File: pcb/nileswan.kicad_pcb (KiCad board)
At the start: 4 copper layers, 61.2 x 36.6 mm, 54 parts, among them J1 Micro_SD_Card_Det_Hirose_DM3AT, J2 Conn_01x06, U1 ICE40HX1K-VQ100, U2 W25Q16JVZPIQ, U3 AP2127N-1.2, U4 IS66WVE4M16EBLL-70BLI, Y1 AMPMAFB-25.0000T

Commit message: current erata, ibom and PCB changes necessary to manufacture it
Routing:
- net GND: vias 47 -> 49
- added copper zone on B.Cu, net GND
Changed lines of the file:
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@@
   (via (at 144.44 87.14) (size 0.5) (drill 0.3) (layers "F.Cu" "B.Cu") (net 1))
   (via (at 171 96) (size 0.5) (drill 0.3) (layers "F.Cu" "B.Cu") (net 1))
+  (via (at 158.56 96.01) (size 0.5) (drill 0.3) (layers "F.Cu" "B.Cu") (free) (net 1))
   (via (at 172.6 110.3) (size 0.5) (drill 0.3) (layers "F.Cu" "B.Cu") (net 1))
   (via (at 133.1 98.827) (size 0.5) (drill 0.3) (layers "F.Cu" "B.Cu") (net 1))
@@
   (via (at 138.4 86.8) (size 0.5) (drill 0.3) (layers "F.Cu" "B.Cu") (net 1))
   (via (at 164.225 102.9) (size 0.5) (drill 0.3) (layers "F.Cu" "B.Cu") (net 1))
+  (via (at 160.87 98.13) (size 0.5) (drill 0.3) (layers "F.Cu" "B.Cu") (free) (net 1))
   (via (at 152.97 100.33) (size 0.5) (drill 0.3) (layers "F.Cu" "B.Cu") (net 1))
   (via (at 155.2 83.4) (size 0.5) (drill 0.3) (layers "F.Cu" "B.Cu") (net 1))
@@
   (via (at 158.7 93.8) (size 0.45) (drill 0.3) (layers "F.Cu" "B.Cu") (net 62))
   (via (at 128.9 88.5) (size 0.45) (drill 0.3) (layers "F.Cu" "B.Cu") (net 62))
+  (segment (start 157.544512 93.8) (end 156.835012 94.5095) (width 0.127) (layer "B.Cu") (net 62))
   (segment (start 134.4 94) (end 128.9 88.5) (width 0.127) (layer "B.Cu") (net 62))
-  (segment (start 157.92 94.58) (end 157.5765 94.2365) (width 0.127) (layer "B.Cu") (net 62))
+  (segment (start 147.008012 93.8365) (end 146.844512 94) (width 0.127) (layer "B.Cu") (net 62))
   (segment (start 156.835012 94.5095) (end 148.064988 94.5095) (width 0.127) (layer "B.Cu") (net 62))
-  (segment (start 147.008012 93.8365) (end 146.844512 94) (width 0.127) (layer "B.Cu") (net 62))
-  (segment (start 158.7 93.8) (end 157.92 94.58) (width 0.127) (layer "B.Cu") (net 62))
-  (segment (start 157.5765 94.2365) (end 157.108012 94.2365) (width 0.127) (layer "B.Cu") (net 62))
-  (segment (start 157.108012 94.2365) (end 156.835012 94.5095) (width 0.127) (layer "B.Cu") (net 62))
   (segment (start 146.844512 94) (end 134.4 94) (width 0.127) (layer "B.Cu") (net 62))
   (segment (start 147.391988 93.8365) (end 147.008012 93.8365) (width 0.127) (layer "B.Cu") (net 62))
   (segment (start 148.064988 94.5095) (end 147.391988 93.8365) (width 0.127) (layer "B.Cu") (net 62))
+  (segment (start 158.7 93.8) (end 157.544512 93.8) (width 0.127) (layer "B.Cu") (net 62))
   (segment (start 129.869 86.25) (end 130.1 86.25) (width 0.127) (layer "F.Cu") (net 63))
   (segment (start 158.182012 94.3375) (end 166.875 94.3375) (width 0.127) (layer "F.Cu") (net 63))
@@
   (via (at 136.3 98.9) (size 0.45) (drill 0.3) (layers "F.Cu" "B.Cu") (net 83))
   (via (at 165.1 98.3) (size 0.45) (drill 0.3) (layers "F.Cu" "B.Cu") (net 83))
+  (segment (start 152.328 103.238) (end 159.6 103.238) (width 0.127) (layer "B.Cu") (net 83))
+  (segment (start 138.3175 103.1175) (end 152.2075 103.1175) (width 0.127) (layer "B.Cu") (net 83))
+  (segment (start 136.3 101.1) (end 138.3175 103.1175) (width 0.127) (layer "B.Cu") (net 83))
   (segment (start 164.538 98.3) (end 165.1 98.3) (width 0.127) (layer "B.Cu") (net 83))
-  (segment (start 152.384 103.238) (end 159.6 103.238) (width 0.127) (layer "B.Cu") (net 83))
-  (segment (start 136.3 101.1) (end 138.3175 103.1175) (width 0.127) (layer "B.Cu") (net 83))
-  (segment (start 138.3175 103.1175) (end 151.0955 103.1175) (width 0.127) (layer "B.Cu") (net 83))
-  (segment (start 151.0955 103.1175) (end 151.8 103.822) (width 0.127) (layer "B.Cu") (net 83))
+  (segment (start 152.2075 103.1175) (end 152.328 103.238) (width 0.127) (layer "B.Cu") (net 83))
   (segment (start 159.6 103.238) (end 164.538 98.3) (width 0.127) (layer "B.Cu") (net 83))
   (segment (start 136.3 98.9) (end 136.3 101.1) (width 0.127) (layer "B.Cu") (net 83))
-  (segment (start 151.8 103.822) (end 152.384 103.238) (width 0.127) (layer "B.Cu") (net 83))
   (segment (start 163.75 84.25) (end 162.75 84.25) (width 0.127) (layer "F.Cu") (net 86))
   (segment (start 161.2125 88.562026) (end 161.2125 89.175) (width 0.127) (layer "F.Cu") (net 86))
@@
       )
     )
+  )
+  (zone (net 1) (net_name "GND") (layer "B.Cu") (hatch edge 0.5)
+    (priority 2)
+    (connect_pads (clearance 0.5))
+    (min_thickness 0.25) (filled_areas_thickness no)
+    (fill yes (thermal_gap 0.5) (thermal_bridge_width 0.5))
+    (polygon
+      (pts
+        (xy 107.18 77.99)
+        (xy 181.06 77.53)
+        (xy 179.07 121.57)
+        (xy 108.72 121.42)
+      )
+    )

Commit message: second pcb iteration
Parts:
- removed J2: Conn_01x06, Connector_PinSocket_1.27mm:PinSocket_1x06_P1.27mm_Vertical
- removed R14: 10k, Resistor_SMD:R_0603_1608Metric
- removed R20, R21: 2.2k, Resistor_SMD:R_0603_1608Metric
- added C24: 1 μF, Capacitor_SMD:C_0603_1608Metric, F.Cu at (163.1, 106.2)
- added C25: 1 μF, Capacitor_SMD:C_0603_1608Metric, F.Cu at (159.7, 102.7)
- added C26: 100 nF, Capacitor_SMD:C_0402_1005Metric, F.Cu at (129.0, 88.8)
- added C27: 470 pF, Capacitor_SMD:C_0402_1005Metric, F.Cu at (165.1, 103.2)
- added C28: 4.7 nF, Capacitor_SMD:C_0402_1005Metric, F.Cu at (165.1, 104.2)
- added C29: 100 nF, Capacitor_SMD:C_0402_1005Metric, F.Cu at (127.6, 85.5)
- added C30: 100 nF, Capacitor_SMD:C_0402_1005Metric, F.Cu at (125.5, 88.1)
- added C31: 100 nF, Capacitor_SMD:C_0402_1005Metric, F.Cu at (129.8, 97.2)
- added J3: SM02B-SRSS-TB_LF__SN_, snapeda:SM02B-SRSS-TB_LF__SN_, F.Cu at (133.9, 86.6)
- added J4: Conn_02x05_Counter_Clockwise, Connector:Tag-Connect_TC2050-IDC-NL_2x05_P1.27mm_Vertical, B.Cu at (133.4, 85.5)
- added R3: 47k, Resistor_SMD:R_0402_1005Metric, F.Cu at (163.4, 101.0)
- added R4: 10k, Resistor_SMD:R_0402_1005Metric, F.Cu at (145.1, 85.9)
- added R6: 10k, Resistor_SMD:R_0402_1005Metric, F.Cu at (139.3, 84.8)
- added R7: 10k, Resistor_SMD:R_0402_1005Metric, F.Cu at (159.4, 103.9)
- added R8: 2.2k, Resistor_SMD:R_0402_1005Metric, F.Cu at (156.1, 85.7)
- added U5: AP22966DC8-7, snapeda:IC_AP22966DC8-7, F.Cu at (162.5, 103.7)
- added U6: IS62WV5128EBLL-45BLI, nileswan:BGA-36_6x8_6.0x8.0mm, F.Cu at (129.4, 93.0)
- added U7: TPS3613, Package_SO:VSSOP-10_3x3mm_P0.5mm, F.Cu at (124.0, 85.4)
- C10, C12, C14, C15, C16, C17, C18, C19, C2, C20, C21, C22, C23, C3, C4, C5, C6, C7, C8, C9: footprint Capacitor_SMD:C_0603_1608Metric -> Capacitor_SMD:C_0402_1005Metric
- D1, D2, D3, D4, D5: footprint LED_SMD:LED_0603_1608Metric -> LED_SMD:LED_0402_1005Metric
- R10, R15, R16, R17, R2, R23, R9: footprint Resistor_SMD:R_0603_1608Metric -> Resistor_SMD:R_0402_1005Metric
- R11, R12, R13: value 10k -> 2.2k; footprint Resistor_SMD:R_0603_1608Metric -> Resistor_SMD:R_0402_1005Metric
- R18: value 2.2k -> 118k; footprint Resistor_SMD:R_0603_1608Metric -> Resistor_SMD:R_0402_1005Metric
- R19: value 2.2k -> 75k; footprint Resistor_SMD:R_0603_1608Metric -> Resistor_SMD:R_0402_1005Metric
- R5: value 47k -> 10k; footprint Resistor_SMD:R_0603_1608Metric -> Resistor_SMD:R_0402_1005Metric
- U2: value W25Q16JVZPIQ -> W25Q16JVUXIQ; footprint snapeda:SON127P500X600X80-9N -> snapeda:SON50P300X200X60-9N
- moved J1 42.8 mm to (165.1, 91.2), turned to 180 degrees
- moved R10 40.8 mm to (162.3, 101.0), turned to 90 degrees
- moved R9 38.7 mm to (156.2, 89.5), turned to -90 degrees
- moved R23 38.6 mm to (134.1, 104.2)
- moved C1 36.6 mm to (166.7, 101.1), turned to 0 degrees
- moved R5 33.5 mm to (145.6, 83.6)
- moved C11 30.9 mm to (158.2, 105.8), turned to 0 degrees
- moved U3 27.4 mm to (156.2, 104.8), turned to -90 degrees
- moved C15 26.9 mm to (141.1, 105.1), turned to -90 degrees
- moved C14 24.4 mm to (148.1, 86.0), turned to 90 degrees
- moved C13 24.2 mm to (153.7, 104.7)
- moved R15 22.0 mm to (156.1, 86.7)
- moved C19 20.7 mm to (137.0, 94.9), turned to 180 degrees
- moved R18 18.3 mm to (120.2, 84.7), turned to -90 degrees
- moved D1 17.6 mm to (154.0, 86.6), turned to 180 degrees
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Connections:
- net Net-(U1C-CRESET_B) renamed /fpga/CRESET_B
- net Net-(U3-VO) renamed 1.2V
- C1 pad 1: 3.3V -> 3.3V_TF
- J1 pad 10: /fpga/SD_DETECT -> /fpga/TF_DETECT
- J1 pad 2: Net-(J1-DAT3/CD) -> /fpga/TF_SEL
- J1 pad 3: /fpga/SD_CMD -> /fpga/TF_PICO
- J1 pad 4: 3.3V -> 3.3V_TF
- J1 pad 5: /fpga/SD_CLK -> /fpga/TF_CLK
- J1 pad 7: /fpga/SD_DAT0 -> /fpga/TF_POCI
- R1 pad 1: 3.3V -> Net-(U5-VBIAS)
- R10 pad 1: 3.3V -> 3.3V_TF
- R11 pad 1: 3.3V -> GND
- R11 pad 2: Net-(J2-Pin_3) -> Net-(D3-K)
- R12 pad 1: 3.3V -> GND
- R12 pad 2: Net-(U2-IO3) -> Net-(D4-K)
- R13 pad 1: 3.3V -> GND
- R13 pad 2: Net-(J2-Pin_4) -> Net-(D5-K)
- R15 pad 1: Net-(D1-K) -> GND
- R15 pad 2: GND -> Net-(D1-K)
- R18 pad 1: GND -> 3.3V
- R18 pad 2: Net-(D2-K) -> Net-(U7-SENSE)
- R19 pad 1: GND -> Net-(U7-SENSE)
- R19 pad 2: Net-(D3-K) -> GND
- R5 pad 2: Net-(J1-DAT1) -> Net-(U2-/WP)
- R9 pad 1: 3.3V -> 3.3V_TF
- R9 pad 2: Net-(J1-DAT3/CD) -> /fpga/TF_POCI
- U1 pad 1: /fpga/A_HIGH0 -> /fpga/A16
- U1 pad 10: /fpga/ENABLE_OUT_PSRAM -> /fpga/MBC
- U1 pad 100: unconnected-(U1A-IOT_95-Pad100) -> /fpga/A17
- U1 pad 12: /fpga/SD_DETECT -> /fpga//IO
- U1 pad 13: unconnected-(U1D-IOL_6B_GBIN7-Pad13) -> /fpga//WE
- U1 pad 15: unconnected-(U1D-IOL_7A_GBIN6-Pad15) -> /fpga/SCLK
- U1 pad 16: /fpga/SD_CMD -> /fpga//SEL
- U1 pad 18: /fpga/SD_DAT0 -> /fpga/TF_POW
- U1 pad 19: /fpga/SD_CLK -> /fpga/TF_SEL
- U1 pad 2: /fpga/A_HIGH1 -> /fpga/D8
- U1 pad 20: Net-(D2-A) -> /fpga/TF_PICO
- U1 pad 21: Net-(D3-A) -> /fpga/TF_CLK
- U1 pad 24: Net-(D4-A) -> /fpga/TF_POCI
- U1 pad 25: Net-(D5-A) -> /fpga/TF_DETECT
- U1 pad 26: unconnected-(U1C-IOB_26-Pad26) -> Net-(D2-A)
- U1 pad 27: unconnected-(U1C-IOB_27-Pad27) -> Net-(D3-A)
- U1 pad 28: unconnected-(U1C-IOB_28-Pad28) -> Net-(D4-A)
- U1 pad 29: unconnected-(U1C-IOB_29-Pad29) -> Net-(D5-A)
- U1 pad 3: /fpga/A_HIGH2 -> /fpga/D9
- U1 pad 4: /fpga/A_HIGH3 -> /fpga/D10
- U1 pad 45: Net-(J2-Pin_1) -> /fpga/FLASH_PICO
- U1 pad 46: Net-(J2-Pin_2) -> /fpga/FLASH_POCI
- U1 pad 48: Net-(J2-Pin_3) -> /fpga/FLASH_CLK
- U1 pad 49: Net-(J2-Pin_4) -> /fpga/FLASH_CS
- U1 pad 51: /fpga/A7 -> unconnected-(U1B-IOR_52-Pad51)
- U1 pad 52: /fpga/A6 -> /fpga/A_HIGH0
- U1 pad 53: /fpga/A5 -> /fpga/A_HIGH1
- U1 pad 54: /fpga/A4 -> /fpga/A_HIGH2
- U1 pad 56: /fpga/D15 -> /fpga/A_HIGH3
- U1 pad 57: /fpga/D14 -> /fpga/A_HIGH4
- U1 pad 59: /fpga/D7 -> /fpga/A_HIGH5
- U1 pad 60: /fpga/D6 -> /fpga/A_HIGH6
- U1 pad 64: /fpga/D5 -> /fpga//SEL_SRAM
- U1 pad 65: /fpga/D4 -> /fpga//SEL_PSRAM
- U1 pad 66: /fpga/D3 -> /fpga//PSRAM_UB
- U1 pad 68: /fpga/D2 -> /fpga//PSRAM_LB
- U1 pad 69: /fpga/D1 -> /fpga/A8
- U1 pad 7: /fpga/A_HIGH4 -> /fpga/D11
- U1 pad 71: /fpga/D0 -> /fpga/A7
- U1 pad 72: /fpga/A0 -> /fpga/A6
- U1 pad 73: /fpga/A1 -> /fpga/A5
- U1 pad 74: /fpga/A2 -> /fpga/A4
- U1 pad 78: /fpga/A3 -> /fpga/D15
- U1 pad 79: /fpga/A19 -> /fpga/D14
- U1 pad 8: /fpga/A_HIGH5 -> /fpga/D12
- U1 pad 80: /fpga/A18 -> /fpga/D7
- U1 pad 81: /fpga/A17 -> /fpga/D6
- U1 pad 82: /fpga/A16 -> /fpga/D5
- U1 pad 83: /fpga/D8 -> /fpga/D4
- U1 pad 85: /fpga/D9 -> /fpga/D3
- U1 pad 86: /fpga/D10 -> /fpga/D2
- U1 pad 87: /fpga/D11 -> /fpga/D1
- U1 pad 89: /fpga/SCLK -> unconnected-(U1A-IOT_84_GBIN1-Pad89)
- U1 pad 9: /fpga//SEL_PSRAM -> /fpga/D13
- U1 pad 90: unconnected-(U1A-IOT_85_GBIN0-Pad90) -> /fpga//OE
- U1 pad 91: /fpga/D12 -> /fpga/D0
- U1 pad 93: /fpga/D13 -> /fpga/A0
- U1 pad 94: /fpga/MBC -> /fpga/A1
- U1 pad 95: /fpga//IO -> /fpga/A2
- U1 pad 96: /fpga//OE -> /fpga/A3
- U1 pad 97: /fpga//WE -> /fpga/A19
- U1 pad 99: /fpga//SEL -> /fpga/A18
- U2 pad 1: Net-(J2-Pin_4) -> /fpga/FLASH_CS
- U2 pad 2: Net-(J2-Pin_2) -> /fpga/FLASH_PICO
- U2 pad 5: Net-(J2-Pin_1) -> /fpga/FLASH_POCI
- U2 pad 6: Net-(J2-Pin_3) -> /fpga/FLASH_CLK
- U4 pad A1: /fpga/ENABLE_OUT_PSRAM -> /fpga//PSRAM_LB
- U4 pad A3: /fpga/A0 -> /fpga/A1
- U4 pad A4: /fpga/A1 -> /fpga/A2
- U4 pad A5: /fpga/A2 -> /fpga/A3
- U4 pad B2: /fpga/ENABLE_OUT_PSRAM -> /fpga//PSRAM_UB
- U4 pad B3: /fpga/A3 -> /fpga/A4
- U4 pad B4: /fpga/A4 -> /fpga/A5
- U4 pad C3: /fpga/A5 -> /fpga/A6
- U4 pad C4: /fpga/A6 -> /fpga/A7
- U4 pad D3: /fpga/A_HIGH1 -> /fpga/A_HIGH2
- U4 pad D4: /fpga/A7 -> /fpga/A8
- U4 pad E3: /fpga/A_HIGH5 -> /fpga/A_HIGH6
- U4 pad E4: /fpga/A_HIGH0 -> /fpga/A_HIGH1
- U4 pad F3: /fpga/A14 -> /fpga/A15
- U4 pad F4: /fpga/A15 -> /fpga/A_HIGH0
- U4 pad G2: /fpga/A_HIGH3 -> /fpga/A_HIGH4
- U4 pad G3: /fpga/A12 -> /fpga/A13
- U4 pad G4: /fpga/A13 -> /fpga/A14
- U4 pad H1: /fpga/A_HIGH2 -> /fpga/A_HIGH3
- U4 pad H2: /fpga/A8 -> /fpga/A9
- U4 pad H3: /fpga/A9 -> /fpga/A10
- U4 pad H4: /fpga/A10 -> /fpga/A11
- U4 pad H5: /fpga/A11 -> /fpga/A12
- U4 pad H6: /fpga/A_HIGH4 -> /fpga/A_HIGH5
- Y1 pad 1: Net-(U1C-IOB_36_GBIN4) -> Net-(U1C-IOB_34)
- Y1 pad 3: Net-(U1C-IOB_34) -> Net-(U1C-IOB_36_GBIN4)
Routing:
- net /fpga/SD_DETECT: track 56.6 -> 0.00 mm, vias 2 -> 0
- net /fpga/SD_DAT0: track 43.8 -> 0.00 mm, vias 2 -> 0
- net /fpga/SD_CLK: track 42.1 -> 0.00 mm, vias 2 -> 0
- net /fpga/SD_CMD: track 41.2 -> 0.00 mm, vias 2 -> 0
- net /fpga/ENABLE_OUT_PSRAM: track 38.4 -> 0.00 mm, vias 2 -> 0
- net Net-(J2-Pin_4): track 37.1 -> 0.00 mm, vias 3 -> 0
- net Net-(J2-Pin_3): track 37.1 -> 0.00 mm, vias 1 -> 0
- net /fpga/A_HIGH4: track 57.7 -> 21.9 mm
- net /fpga//OE: track 43.5 -> 78.2 mm, vias 2 -> 4
- net Net-(J2-Pin_2): track 34.6 -> 0.00 mm, vias 3 -> 0
- net /fpga/D0: track 35.0 -> 67.9 mm, vias 2 -> 3
- net /fpga/D3: track 36.7 -> 68.9 mm, vias 2 -> 3
- net /fpga/A2: track 30.3 -> 61.9 mm, vias 2 -> 4
- net /fpga//SEL_SRAM: track 0.00 -> 31.2 mm, vias 0 -> 2
- net Net-(J2-Pin_1): track 31.1 -> 0.00 mm, vias 1 -> 0
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- added copper zone on F.Cu, net GND
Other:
- board size 61.2 x 36.6 mm -> 61.4 x 36.6 mm
- board text added: "JLCJLCJLCJLC"
- board text added: "nileswan rev 2 github.com/RSDuck/nileswan"
- board text removed: "PICO POCI SCK CS GND 3.3V"
- board text removed: "nileschwan [ʃvan] rev 0.0 github.com/RSDuck/nileswan/"

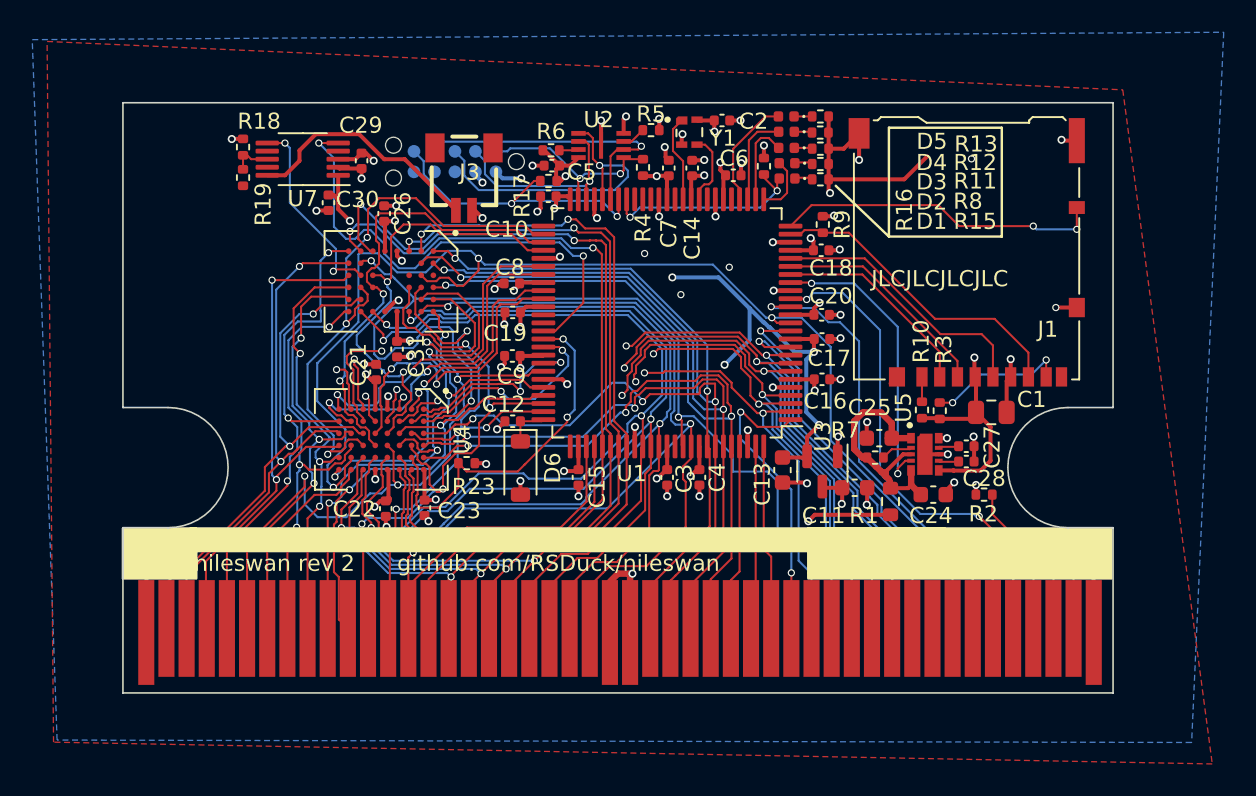
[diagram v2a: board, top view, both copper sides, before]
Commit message: pcb revision 3 and 16 MB PSRAM support
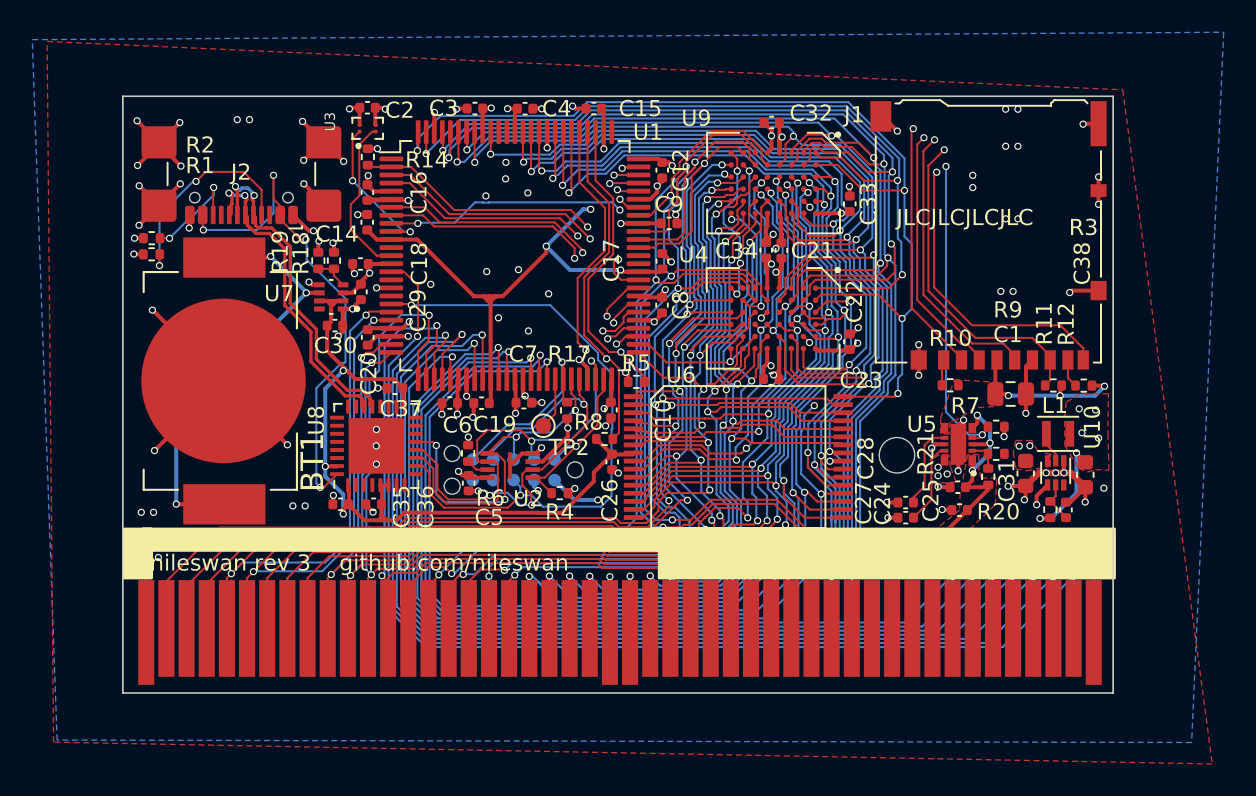
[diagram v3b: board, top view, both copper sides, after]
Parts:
- removed C11, C13: 1 μF, Capacitor_SMD:C_0603_1608Metric
- removed D1, D2, D3, D4, D5: LED, LED_SMD:LED_0402_1005Metric
- removed D6: 1N5819, Diode_SMD:D_SOD-123
- removed J3: SM02B-SRSS-TB_LF__SN_, snapeda:SM02B-SRSS-TB_LF__SN_
- removed R13, R16: 2.2k, Resistor_SMD:R_0402_1005Metric
- removed R15: 22, Resistor_SMD:R_0402_1005Metric
- removed R23: 10k, Resistor_SMD:R_0402_1005Metric
- removed Y1: AMPMAFB-25.0000T, snapeda:XTAL_AMPMAFB-25.0000T
- added BT1: Battery_Cell, snapeda:BAT_BAT-HLD-012-SMT, F.Cu at (119.0, 99.2)
- added C32: 100 nF, Capacitor_SMD:C_0402_1005Metric, F.Cu at (153.0, 83.1)
- added C33: 100 nF, Capacitor_SMD:C_0402_1005Metric, F.Cu at (157.9, 88.2)
- added C34: 100 nF, Capacitor_SMD:C_0402_1005Metric, F.Cu at (153.6, 91.1)
- added C35: 100 nF, Capacitor_SMD:C_0402_1005Metric, F.Cu at (126.3, 106.8)
- added C36: 100 nF, Capacitor_SMD:C_0402_1005Metric, F.Cu at (128.3, 106.8)
- added C37: 100 nF, Capacitor_SMD:C_0402_1005Metric, F.Cu at (129.7, 99.6)
- added C38: 22 μF, Capacitor_SMD:C_0603_1608Metric, F.Cu at (172.5, 105.0)
- added J2: USB_C_Receptacle_USB2.0, Connector_USB:USB_C_Receptacle_GCT_USB4110, F.Cu at (120.2, 85.2)
- added L1: 1 μH, Inductor_SMD:L_Murata_DFE201610P, F.Cu at (170.8, 102.4)
- added R14: 10k, Resistor_SMD:R_0402_1005Metric, F.Cu at (128.0, 85.3)
- added R20: TBD, Resistor_SMD:R_0402_1005Metric, F.Cu at (166.5, 105.1)
- added R21: TBD, Resistor_SMD:R_0402_1005Metric, F.Cu at (166.9, 103.7)
- added REF**: MountingHole_2.2mm_M2, MountingHole:MountingHole_2.2mm_M2, F.Cu at (160.8, 103.8)
- added TP2: TestPoint, TestPoint:TestPoint_Pad_D1.0mm, F.Cu at (138.9, 101.9)
- added U10: TPS62A01DRLR, Package_TO_SOT_SMD:SOT-563, F.Cu at (170.6, 104.8)
- added U8: STM32L052K6Ux, Package_DFN_QFN:QFN-32-1EP_5x5mm_P0.5mm_EP3.45x3.45mm, F.Cu at (128.5, 103.2)
- added U9: IS66WVE4M16EBLL-70BLI, nileswan:BGA-48_6x8_6.0x8.0mm, F.Cu at (153.1, 86.9)
- C24, C25: value 1 μF -> 200 nF; footprint Capacitor_SMD:C_0603_1608Metric -> Capacitor_SMD:C_0402_1005Metric
- C31: value 100 nF -> 4.7 μF; footprint Capacitor_SMD:C_0402_1005Metric -> Capacitor_SMD:C_0603_1608Metric
- R1: value 1 -> 5.1k; footprint Resistor_SMD:R_0603_1608Metric -> Resistor_SMD:R_0402_1005Metric
- R11, R8: value 2.2k -> 100k
- R12: value 2.2k -> 100k; footprint Resistor_SMD:R_0402_1005Metric -> Capacitor_SMD:C_0402_1005Metric
- R18: value 118k -> 1.16M
- R19: value 75k -> 610k
- R2: value 10k -> 5.1k
- U3: value AP2127N-1.2 -> SIT8021AI-J4-XXS-24.000000E; footprint Package_TO_SOT_SMD:SOT-23 -> snapeda:BGA4N41X100P2X2_84X154X60N
- U6: value IS62WV5128EBLL-45BLI -> RMLV0408EGSA-4S2; footprint nileswan:BGA-36_6x8_6.0x8.0mm -> nileswan:sTSOP-32
- U7: value TPS3613 -> TPS2117; footprint Package_SO:VSSOP-10_3x3mm_P0.5mm -> snapeda:SOTFL50P160X60-8N
- moved R2 54.0 mm to (114.6, 90.3)
- moved R1 48.3 mm to (114.6, 91.3), turned to 0 degrees
- moved C31 39.7 mm to (168.8, 104.9), turned to -90 degrees
- moved U3 35.3 mm to (128.0, 83.5), turned to 90 degrees
- moved C22 30.6 mm to (157.9, 96.7), turned to -90 degrees
- moved C16 30.5 mm to (128.0, 87.5), turned to 90 degrees
- moved C18 28.6 mm to (127.5, 91.9), turned to 180 degrees
- moved C20 28.2 mm to (128.0, 96.5), turned to -90 degrees
- moved R12 27.9 mm to (171.3, 107.2), turned to 90 degrees
- moved R11 26.5 mm to (170.3, 107.1), turned to 90 degrees
- moved C3 25.8 mm to (134.6, 82.3), turned to 180 degrees
- moved U4 25.4 mm to (153.1, 95.3)
- moved C21 25.3 mm to (152.7, 91.0)
- moved C4 25.3 mm to (137.7, 82.3), turned to 0 degrees
- moved U6 24.1 mm to (151.0, 103.9)
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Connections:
- B1 pad 24: Net-(B1-Vdd-Pad24) -> 3.3V_PROG
- B1 pad 25: Net-(B1-Vdd-Pad24) -> 3.3V_PROG
- B1 pad 46: Net-(B1-/CARTINT) -> /fpga//CARTINT
- C12 pad 1: Net-(D6-K) -> 3.3V
- C24 pad 1: Net-(U5-VBIAS) -> 3.3V_PROG
- C25 pad 1: Net-(U5-VBIAS) -> 3.3V_PROG
- C31 pad 1: GND -> 3.3V
- C31 pad 2: 3.3V_SRAM -> GND
- J1 pad 10: /fpga/TF_DETECT -> GND
- J1 pad 9: unconnected-(J1-DET_B-Pad9) -> /fpga/TF_DETECT
- J4 pad 1: 3.3V -> 3.3V_PROG
- J4 pad 3: unconnected-(J4-Pin_3-Pad3) -> /fpga//μC_CS
- J4 pad 7: /fpga/FLASH_PICO -> /fpga/FLASH_POCI
- J4 pad 8: /fpga/FLASH_POCI -> /fpga/FLASH_PICO
- R1 pad 1: Net-(U5-VBIAS) -> GND
- R1 pad 2: Net-(B1-Vdd-Pad24) -> Net-(J2-CC1)
- R11 pad 1: GND -> 1.2V
- R11 pad 2: Net-(D3-K) -> Net-(U10-FB)
- R12 pad 1: GND -> Net-(U10-FB)
- R12 pad 2: Net-(D4-K) -> GND
- R18 pad 2: Net-(U7-SENSE) -> Net-(U7-PR1)
- R19 pad 1: Net-(U7-SENSE) -> Net-(U7-PR1)
- R2 pad 1: 3.3V -> GND
- R2 pad 2: Net-(B1-/CARTINT) -> Net-(J2-CC2)
- R5 pad 2: Net-(U2-/WP) -> /fpga//SEL_PSRAM1
- R7 pad 1: Net-(U5-VBIAS) -> GND
- R7 pad 2: Net-(U5-EN1) -> /fpga/TF_POW
- R8 pad 1: GND -> 3.3V_SRAM
- R8 pad 2: Net-(D2-K) -> /fpga//SEL_SRAM
- U1 pad 1: /fpga/A16 -> unconnected-(U1D-IOL_1A-Pad1)
- U1 pad 10: /fpga/MBC -> Net-(U1D-IOL_5B)
- U1 pad 100: /fpga/A17 -> /fpga//MEM_OE
- U1 pad 12: /fpga//IO -> unconnected-(U1D-IOL_6A-Pad12)
- U1 pad 13: /fpga//WE -> Net-(U1D-IOL_6B_GBIN7)
- U1 pad 16: /fpga//SEL -> unconnected-(U1D-IOL_7B-Pad16)
- U1 pad 18: /fpga/TF_POW -> unconnected-(U1D-IOL_8A-Pad18)
- U1 pad 19: /fpga/TF_SEL -> /fpga//μC_CS
- U1 pad 2: /fpga/D8 -> /fpga//SEL_PSRAM2
- U1 pad 20: /fpga/TF_PICO -> /fpga/A9
- U1 pad 21: /fpga/TF_CLK -> /fpga/A8
- U1 pad 24: /fpga/TF_POCI -> /fpga/A7
- U1 pad 25: /fpga/TF_DETECT -> /fpga/A6
- U1 pad 26: Net-(D2-A) -> /fpga/A5
- U1 pad 27: Net-(D3-A) -> /fpga/A4
- U1 pad 28: Net-(D4-A) -> /fpga//CARTINT
- U1 pad 29: Net-(D5-A) -> /fpga//SEL
- U1 pad 3: /fpga/D9 -> /fpga/D7
- U1 pad 30: unconnected-(U1C-IOB_30-Pad30) -> /fpga//IO
- U1 pad 33: unconnected-(U1C-IOB_35_GBIN5-Pad33) -> /fpga//OE
- U1 pad 34: Net-(U1C-IOB_36_GBIN4) -> /fpga//WE
- U1 pad 36: Net-(U1C-IOB_34) -> /fpga/MBC
- U1 pad 37: unconnected-(U1C-IOB_37-Pad37) -> /fpga/A16
- U1 pad 4: /fpga/D10 -> /fpga/D4
- U1 pad 40: unconnected-(U1C-IOB_41-Pad40) -> /fpga/A17
- U1 pad 41: unconnected-(U1C-IOB_42_CBSEL0-Pad41) -> /fpga/A18
- U1 pad 42: unconnected-(U1C-IOB_43_CBSEL1-Pad42) -> /fpga/A19
- U1 pad 51: unconnected-(U1B-IOR_52-Pad51) -> /fpga//MEM_WE
- U1 pad 52: /fpga/A_HIGH0 -> /fpga/A_HIGH5
- U1 pad 53: /fpga/A_HIGH1 -> /fpga/A_HIGH2
- U1 pad 54: /fpga/A_HIGH2 -> /fpga/A_HIGH1
- U1 pad 56: /fpga/A_HIGH3 -> /fpga/A_HIGH0
- U1 pad 57: /fpga/A_HIGH4 -> /fpga/A_HIGH6
- U1 pad 59: /fpga/A_HIGH5 -> /fpga/A_HIGH4
- U1 pad 60: /fpga/A_HIGH6 -> /fpga/A_HIGH3
- U1 pad 64: /fpga//SEL_SRAM -> /fpga/D15
- U1 pad 65: /fpga//SEL_PSRAM -> /fpga/D13
- U1 pad 66: /fpga//PSRAM_UB -> /fpga/D14
- U1 pad 68: /fpga//PSRAM_LB -> /fpga/D12
- U1 pad 69: /fpga/A8 -> /fpga/TF_POW
- U1 pad 7: /fpga/D11 -> /fpga/D6
- U1 pad 71: /fpga/A7 -> /fpga/TF_POCI
- U1 pad 72: /fpga/A6 -> /fpga/TF_CLK
- U1 pad 73: /fpga/A5 -> /fpga/TF_PICO
- U1 pad 74: /fpga/A4 -> /fpga/TF_SEL
- U1 pad 75: Net-(D6-K) -> 3.3V
- U1 pad 78: /fpga/D15 -> /fpga//SEL_PSRAM1
- U1 pad 79: /fpga/D14 -> /fpga//SEL_SRAM
- U1 pad 8: /fpga/D12 -> /fpga/D5
- U1 pad 80: /fpga/D7 -> /fpga/A0
- U1 pad 81: /fpga/D6 -> /fpga/A3
- U1 pad 82: /fpga/D5 -> /fpga/A2
- U1 pad 83: /fpga/D4 -> /fpga/A1
- U1 pad 85: /fpga/D3 -> /fpga/D0
- U1 pad 86: /fpga/D2 -> /fpga/D1
- U1 pad 87: /fpga/D1 -> /fpga/D2
- U1 pad 9: /fpga/D13 -> /fpga/TF_DETECT
- U1 pad 90: /fpga//OE -> unconnected-(U1A-IOT_85_GBIN0-Pad90)
- U1 pad 91: /fpga/D0 -> /fpga/D3
- U1 pad 93: /fpga/A0 -> /fpga/D11
- U1 pad 94: /fpga/A1 -> /fpga/D10
- U1 pad 95: /fpga/A2 -> /fpga/D9
- U1 pad 96: /fpga/A3 -> /fpga/D8
- U1 pad 97: /fpga/A19 -> /fpga//PSRAM_UB
- U1 pad 99: /fpga/A18 -> /fpga//PSRAM_LB
- U2 pad 2: /fpga/FLASH_PICO -> /fpga/FLASH_POCI
- U2 pad 3: Net-(U2-/WP) -> 3.3V
- U2 pad 5: /fpga/FLASH_POCI -> /fpga/FLASH_PICO
- U3 pad 1: GND -> Net-(U1D-IOL_5B)
- U3 pad 2: 1.2V -> Net-(U1D-IOL_6B_GBIN7)
- U4 pad A2: /fpga//OE -> /fpga//MEM_OE
- U4 pad B5: /fpga//SEL_PSRAM -> /fpga//SEL_PSRAM1
- U4 pad G5: /fpga//WE -> /fpga//MEM_WE
- U5 pad 1_2: Net-(U5-VBIAS) -> 3.3V_PROG
- U5 pad 4: Net-(U5-VBIAS) -> 3.3V_PROG
- U5 pad 6_7: Net-(U5-VBIAS) -> 3.3V_PROG
- U7 pad 1: 3.3V_SRAM -> GND
- U7 pad 2: 3.3V -> 3.3V_SRAM
- U7 pad 3: GND -> 3.3V
- U7 pad 4: unconnected-(U7-/MR-Pad4) -> Net-(U7-PR1)
- U7 pad 5: /fpga//SEL_SRAM -> 3.3V
- U7 pad 6: /memory//SEL_SRAM -> Net-(BT1-+)
- U7 pad 7: unconnected-(U7-RESET-Pad7) -> 3.3V_SRAM
- U7 pad 8: Net-(U7-SENSE) -> unconnected-(U7-ST-Pad8)
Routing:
- net /fpga//CARTINT: track 0.00 -> 68.7 mm, vias 0 -> 2
- net /fpga//MEM_OE: track 0.00 -> 65.4 mm, vias 0 -> 4
- net /fpga/A9: track 32.0 -> 88.5 mm, vias 3 -> 6
- net /fpga/A4: track 37.6 -> 90.9 mm, vias 4 -> 6
- net 3.3V_PROG: track 0.00 -> 51.5 mm, vias 0 -> 7
- net /fpga/A8: track 42.2 -> 92.1 mm, vias 4 -> 6
- net /fpga/A5: track 38.6 -> 87.8 mm, vias 4 -> 6
- net GND: track 84.8 -> 130.2 mm, vias 61 -> 119
- net /fpga//PSRAM_LB: track 11.8 -> 52.1 mm, vias 2 -> 3
- net /fpga/A10: track 33.2 -> 72.9 mm, vias 2 -> 4
- net /fpga/A18: track 11.4 -> 51.0 mm, vias 0 -> 2
- net /fpga/A17: track 11.5 -> 50.9 mm, vias 0 -> 2
- net /fpga//μC_CS: track 0.00 -> 39.3 mm, vias 0 -> 2
- net /fpga/A13: track 28.0 -> 67.2 mm, vias 3 -> 4
- net /fpga/A15: track 33.2 -> 71.5 mm, vias 2 -> 4
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- added copper zone on F.Cu, net 1.2V
- added copper zone on In2.Cu, net 1.2V
- added copper zone on F.Cu, net 3.3V
- added copper zone on F.Cu, net 3.3V_PROG
- added copper zone on F.Cu, net 3.3V_TF
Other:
- board size 61.4 x 36.6 mm -> 61.4 x 37 mm
- board text added: "Enclosure starts here"
- board text added: "USB Differential Pair assumes JLCPCB JLC04081H-7628 Stackup"
- board text added: "nileswan rev 3 github.com/nileswan"
- board text removed: "nileswan rev 2 github.com/RSDuck/nileswan"
